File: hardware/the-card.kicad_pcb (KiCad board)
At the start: 4 copper layers, 54 x 85.6 mm, 75 parts, among them J1 TYPE-C-31-M-12, J2 FH12-24S-0.5SH(55), J3 BATTERY 1S JST-PH, Q1 SI2301CDS-T1-GE3, Q2 SI2301CDS-T1-GE3, Q3 Si1304BDL, SW1 TS-1187A-B-A-B, SW2 TS-1187A-B-A-B, SW3 TS-1187A-B-A-B, SW4 TS-1187A-B-A-B, U1 ESP32-S3-WROOM-1-N8R2, U10 USBLC6-2SC6, U2 ST25DV04KC-IE8S3, U3 LSM6DSOTR, U4 SHT40-BD1B-R2, U5 MAX17048G+T10, U6 TP4056_C382139, U7 DW01A_C18164398, U8 FS8205A, U9 ME6211C33M5G-N

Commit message: feat(hardware): route pcb layout
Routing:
- net NFC_ANTENNA: track 0.00 -> 228.5 mm, vias 0 -> 2
- net +BAT: track 0.00 -> 180.1 mm, vias 0 -> 14
- net Net-(J3-Pin_2): track 0.00 -> 76.3 mm, vias 0 -> 2
- net I2C_SCL: track 0.00 -> 73.0 mm, vias 0 -> 8
- net USB_DP: track 0.00 -> 72.9 mm, vias 0 -> 2
- net USB_DM: track 0.00 -> 72.9 mm, vias 0 -> 2
- net EPD_VCI: track 0.00 -> 72.6 mm, vias 0 -> 8
- net I2C_SDA: track 0.00 -> 72.5 mm, vias 0 -> 4
- net EPD_SDA: track 0.00 -> 71.1 mm, vias 0 -> 7
- net EPD_DC: track 0.00 -> 70.9 mm, vias 0 -> 4
- net ~CHRG: track 0.00 -> 70.1 mm, vias 0 -> 2
- net BTN_MENU: track 0.00 -> 62.6 mm, vias 0 -> 1
- net VBUS: track 0.00 -> 61.9 mm, vias 0 -> 7
- net EPD_CS: track 0.00 -> 61.4 mm, vias 0 -> 5
- net EPD_BUSY: track 0.00 -> 61.4 mm, vias 0 -> 5
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- added copper zone on In2.Cu, net +3V3
- removed copper zone on In2.Cu, net GND

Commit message: fix(hardware): harden design for fabrication
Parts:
- R10: value 2k -> 1k
- R9: value 470 -> 100
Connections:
- U8 pad 4: Net-(U7-COUT) -> Net-(U7-DOUT)
- U8 pad 5: Net-(U7-DOUT) -> Net-(U7-COUT)
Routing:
- net Net-(U7-DOUT): track 14.2 -> 11.5 mm, vias 0 -> 2
- net Net-(U7-VDD): track 9.50 -> 10.1 mm
- net Net-(U7-COUT): track 11.8 -> 11.6 mm, vias 2 -> 0
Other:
- board text added: "BAT+"
- board text added: "BAT-"
- board text added: "J2 PIN 1"

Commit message: feat(hardware): embed pcb layer reference views
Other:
- board text added: "COPPER LAYER REFERENCE VIEWS - NON-FABRICATION"
- board text added: "L1 F.Cu"
- board text added: "L2 In1.Cu"
- board text added: "L3 In2.Cu"
- board text added: "L4 B.Cu"

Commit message: feat(hardware): add fabrication release workflow
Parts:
- C1, C10, C11, C12, C14, C15, C16, C17, C18, C19, C4, C7: footprint C_0402_1005Metric -> Capacitor_SMD:C_0402_1005Metric
- C13, C2, C3, C5, C6, C8, C9: footprint C_0603_1608Metric -> Capacitor_SMD:C_0603_1608Metric
- C20, C21, C22, C23, C24, C25, C26, C27, C28: footprint C_0805_2012Metric -> Capacitor_SMD:C_0805_2012Metric
- D1: footprint LED-SMD_4P-L3.5-W3.5-TL_WS2812B -> the-card:LED-SMD_4P-L3.5-W3.5-TL_WS2812B
- D2, D3, D4: footprint D_SOD-123 -> Diode_SMD:D_SOD-123
- J1: footprint USB-C_SMD-TYPE-C-31-M-12_1 -> the-card:USB-C_SMD-TYPE-C-31-M-12_1
- J2: footprint Hirose_FH12-24S-0.5SH_1x24-2MP_P0.50mm_Horizontal -> the-card:Hirose_FH12-24S-0.5SH_1x24-2MP_P0.50mm_Horizontal
- J3: footprint JST_PH_S2B-PH-K_1x02_P2.00mm_Horizontal -> Connector_JST:JST_PH_S2B-PH-K_1x02_P2.00mm_Horizontal
- L1: footprint L_Bourns_SRU5016_5.2x5.2mm -> Inductor_SMD:L_Bourns_SRU5016_5.2x5.2mm
- Q1, Q2: footprint SOT-23-3_L3.0-W1.7-P0.95-LS2.9-BR -> the-card:SOT-23-3_L3.0-W1.7-P0.95-LS2.9-BR
- Q3: footprint SOT-323_SC-70 -> Package_TO_SOT_SMD:SOT-323_SC-70
- R1, R10, R11, R12, R13, R14, R15, R16, R2, R3, R4, R5, R6, R7, R8, R9: footprint R_0402_1005Metric -> Resistor_SMD:R_0402_1005Metric
- SW1, SW2, SW3, SW4: footprint SW-SMD_4P-L5.1-W5.1-P3.70-LS6.5-TL_H1.5 -> the-card:SW-SMD_4P-L5.1-W5.1-P3.70-LS6.5-TL_H1.5
- TP1, TP2, TP3, TP4, TP5, TP6: footprint TestPoint_Pad_D1.0mm -> TestPoint:TestPoint_Pad_D1.0mm
- U1: footprint WIRELM-SMD_ESP32-S3-WROOM-1 -> the-card:WIRELM-SMD_ESP32-S3-WROOM-1
- U10: footprint SOT-23-6_L2.9-W1.6-P0.95-LS2.8-BL -> the-card:SOT-23-6_L2.9-W1.6-P0.95-LS2.8-BL
- U2: footprint SO-8_L4.9-W3.9-P1.27-LS6.0-BL -> the-card:SO-8_L4.9-W3.9-P1.27-LS6.0-BL
- U3: footprint LGA-14_L3.0-W2.5-P0.50-TL -> the-card:LGA-14_L3.0-W2.5-P0.50-TL
- U4: footprint DFN-4_L1.5-W1.5-P0.80-TL-EP -> the-card:DFN-4_L1.5-W1.5-P0.80-TL-EP
- U5: footprint TDFN-8_L2.0-W2.0-P0.50-BL-EP1.2 -> the-card:TDFN-8_L2.0-W2.0-P0.50-BL-EP1.2
- U6: footprint ESOP-8_L4.9-W3.9-P1.27-LS6.0-BL-EP -> the-card:ESOP-8_L4.9-W3.9-P1.27-LS6.0-BL-EP
- U7: footprint SOT-23-6_L2.9-W1.6-P0.95-LS2.8-BR -> the-card:SOT-23-6_L2.9-W1.6-P0.95-LS2.8-BR
- U8: footprint TSSOP-8_L4.4-W3.0-P0.65-LS6.4-BL-2 -> the-card:TSSOP-8_L4.4-W3.0-P0.65-LS6.4-BL-2
- U9: footprint SOT-23-5_L3.0-W1.7-P0.95-LS2.8-BL -> the-card:SOT-23-5_L3.0-W1.7-P0.95-LS2.8-BL

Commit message: feat(hardware): upgrade MCU memory variant
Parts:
- U1: value ESP32-S3-WROOM-1-N8R2 -> ESP32-S3-WROOM-1-N16R8
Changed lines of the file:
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@@
 			)
 		)
-		(property "Value" "ESP32-S3-WROOM-1-N8R2"
+		(property "Value" "ESP32-S3-WROOM-1-N16R8"
 			(at 0 -12.895 0)
 			(layer "B.Fab")
@@
 			)
 		)
-		(property "Datasheet" "https://www.lcsc.com/datasheet/C2913204.pdf"
+		(property "Datasheet" "https://www.lcsc.com/datasheet/C2913202.pdf"
 			(at 0 0 0)
 			(layer "B.Fab")
@@
 			)
 		)
-		(property "LCSC Part" "C2913204"
+		(property "LCSC Part" "C2913202"
 			(at 0 0 0)
 			(layer "B.Fab")

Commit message: fix(hardware): source SMT battery connector and inductor
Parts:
- J3: value BATTERY 1S JST-PH -> S2B-PH-SM4-TB(LF)(SN); footprint Connector_JST:JST_PH_S2B-PH-K_1x02_P2.00mm_Horizontal -> Connector_JST:JST_PH_S2B-PH-SM4-TB_1x02-1MP_P2.00mm_Horizontal
- L1: value SRU5016-470Y 47uH -> XRNR5020-47uH/M 47uH; footprint Inductor_SMD:L_Bourns_SRU5016_5.2x5.2mm -> the-card:IND-SMD_L5.0-W5.0_XRNR5020
- moved J3 3.35 mm to (68.8, 44.0)
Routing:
- net Net-(D4-A): track 22.5 -> 21.6 mm
- net EPD_VCI: track 72.6 -> 72.9 mm, vias 8 -> 6
- net EPD_PWR_EN: track 21.7 -> 21.5 mm, vias 2 -> 4
- net GND: vias 77 -> 74

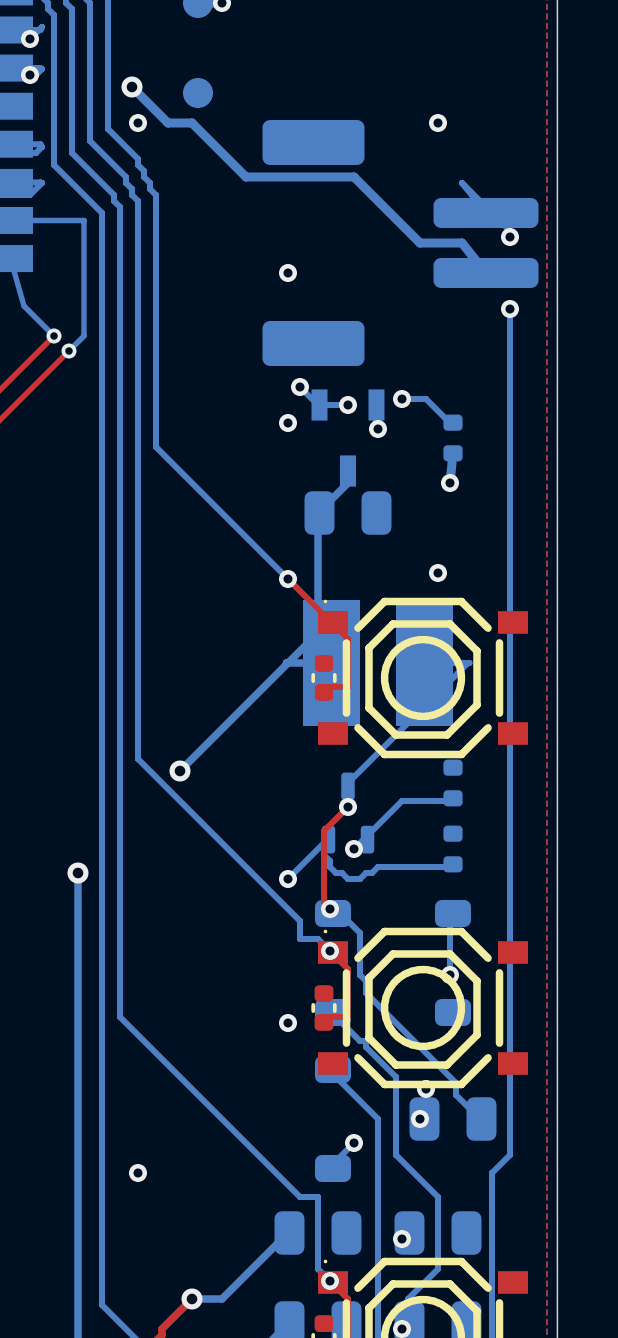
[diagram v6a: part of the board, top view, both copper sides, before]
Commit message: fix(hardware): assign fabrication-ready BOM parts
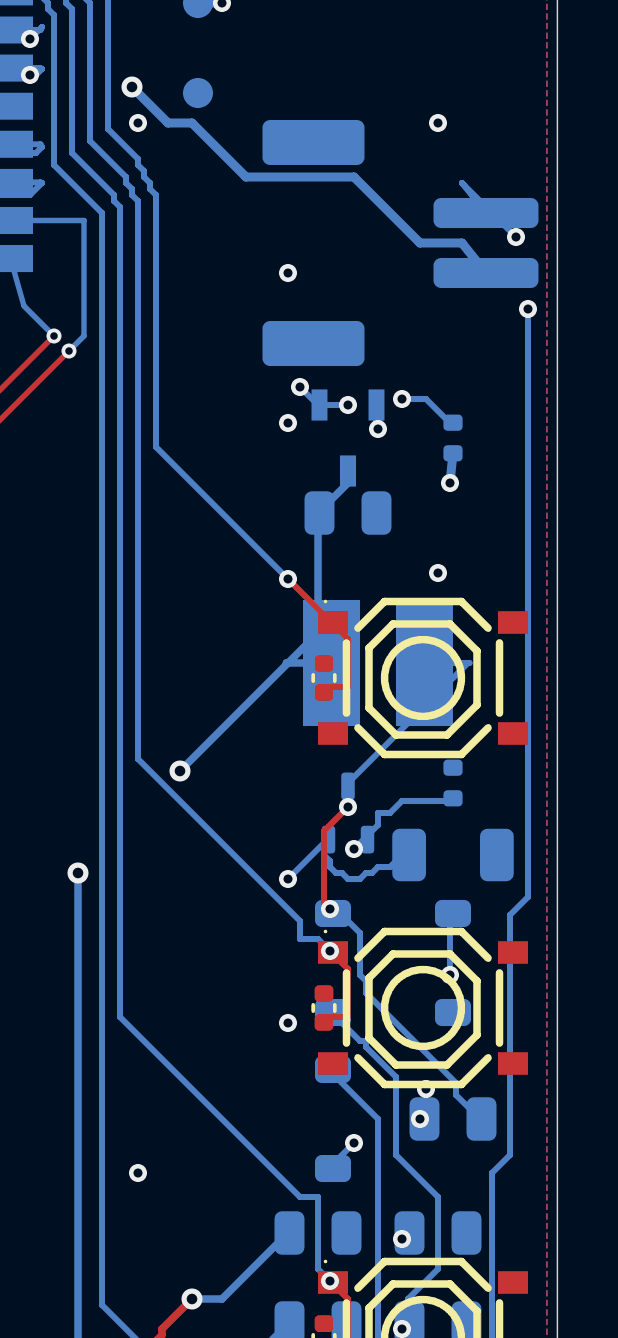
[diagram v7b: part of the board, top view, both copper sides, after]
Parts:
- C22, C23, C24, C25, C26, C27, C28: value 1uF 25V -> 1uF 50V
- D2, D3, D4: value MBR0530 -> LMBR0530T1G
- Q3: value Si1304BDL -> SI1308EDL-T1-GE3
- R16: footprint Resistor_SMD:R_0402_1005Metric -> Resistor_SMD:R_1206_3216Metric
- moved R16 0.20 mm to (70.5, 64.4), turned to 0 degrees
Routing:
- net EPD_RESE: track 59.2 -> 57.9 mm

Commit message: fix(hardware): align U8 fabrication metadata
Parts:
- U8: value FS8205A -> 8205A
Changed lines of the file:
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@@
 			)
 		)
-		(property "Value" "FS8205A"
+		(property "Value" "8205A"
 			(at 0 -7.2 270)
 			(layer "B.Fab")
@@
 			)
 		)
-		(property "Datasheet" "https://lcsc.com/product-detail/MOSFET_FS8205A_C16052.html"
+		(property "Datasheet" "https://www.lcsc.com/datasheet/C5148694.pdf"
 			(at 0 0 270)
 			(layer "B.Fab")
@@
 			)
 		)
-		(property "LCSC Part" "C16052"
+		(property "LCSC Part" "C5148694"
 			(at 0 0 270)
 			(layer "B.Fab")
@@
 			)
 		)
+		(property "MPN" "8205A"
+			(at 0 0 0)
+			(layer "B.SilkS")
+			(hide yes)
+			(effects
+				(font
+					(size 1.27 1.27)
+				)
+			)
+		)
+		(property "Manufacturer" "HXY MOSFET"
+			(at 0 0 0)
+			(layer "B.SilkS")
+			(hide yes)
+			(effects
+				(font
+					(size 1.27 1.27)
+				)
+			)
+		)
